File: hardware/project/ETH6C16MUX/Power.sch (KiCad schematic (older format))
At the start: 27 parts, among them Q701 IRFR5410, U701 OKI-T3-W40P-C, U702 MAX5902, U703 ADP7156ARDZ-3.3-R7, U704 LD1117S12TR_SOT223

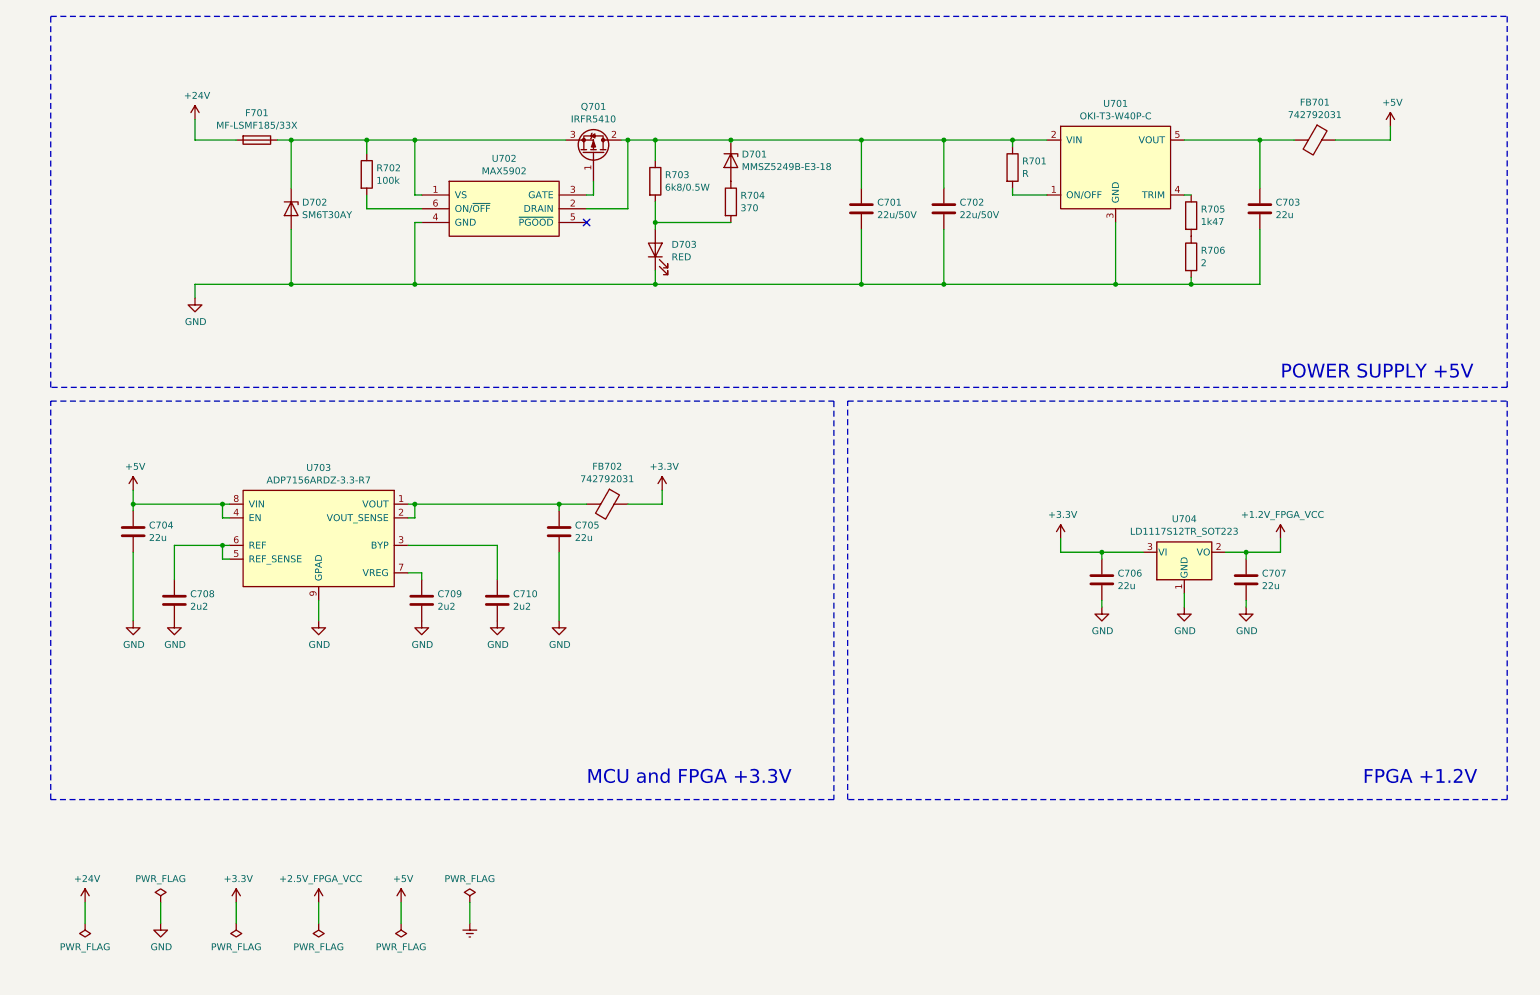
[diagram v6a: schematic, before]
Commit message: PCB layout, deleted USB.
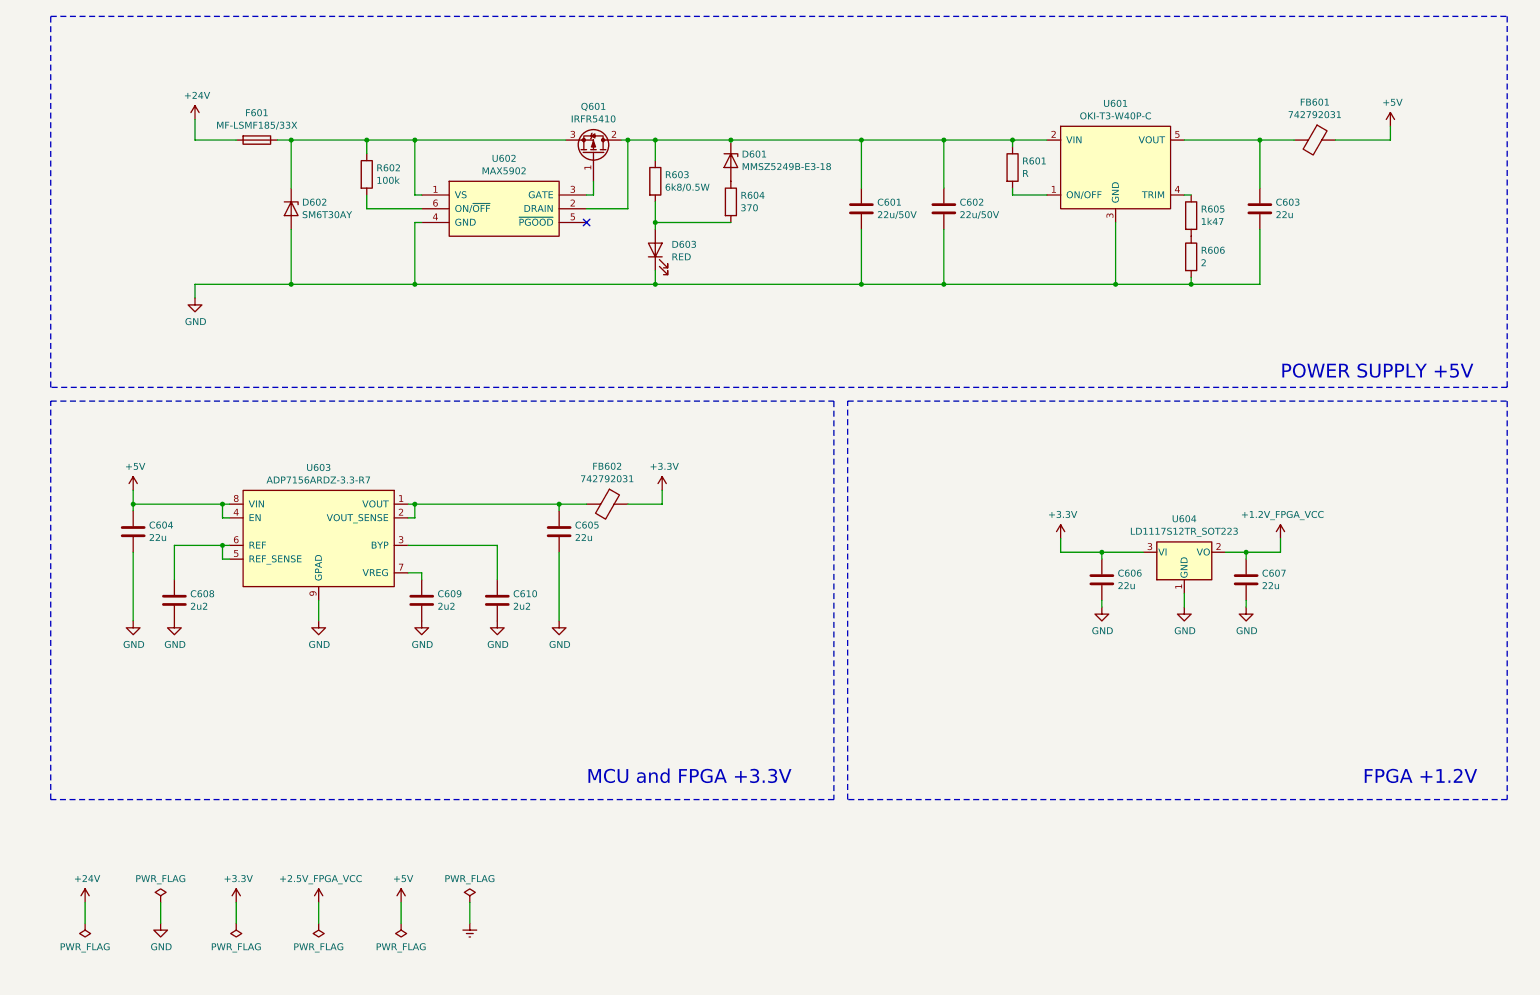
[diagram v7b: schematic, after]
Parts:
- renumbered C701 to C601, C702 to C602, C703 to C603, C704 to C604, C705 to C605, C706 to C606, C707 to C607, C708 to C608, C709 to C609, C710 to C610, D701 to D601, D702 to D602, D703 to D603, F701 to F601, FB701 to FB601, FB702 to FB602, Q701 to Q601, R701 to R601, R702 to R602, R703 to R603, R704 to R604, R705 to R605, R706 to R606, U701 to U601, U702 to U602, U703 to U603, U704 to U604

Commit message: Deleted FPGA part and change it for SPI IO chips. Change power supply circuit.
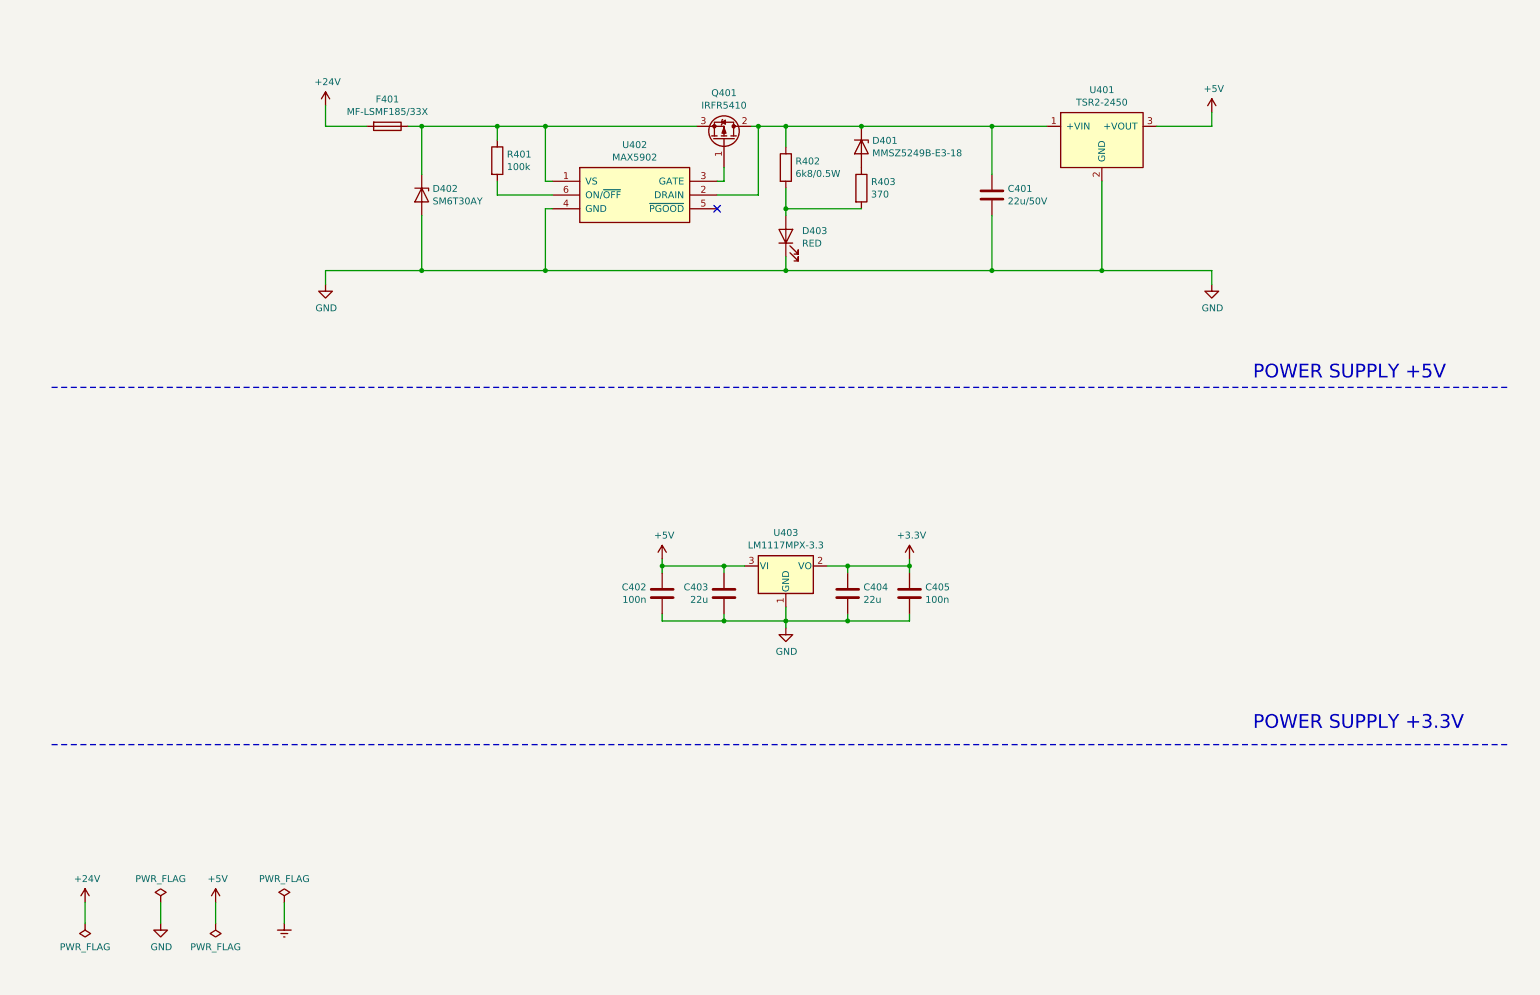
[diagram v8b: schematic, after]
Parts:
- removed C602: 22u/50V, Capacitor_SMD:C_2220_5650Metric_Pad1.97x5.40mm_HandSolder, symbol Device:C
- removed C603, C604, C605, C606, C607: 22u, ETH6C16MXU:C_1210_BB_3225Metric_Pad1.42x2.65mm_HandSolder, symbol Device:C
- removed C608, C609, C610: 2u2, ETH6C16MXU:C_0805_C_Pad1.15x1.40mm_HandSolder, symbol Device:C
- removed FB601, FB602: 742792031, ETH6C16MXU:R_0805_D_Pad1.15x1.40mm_HandSolder, symbol Device:Ferrite_Bead
- removed R601: R, Resistor_SMD:R_0603_1608Metric_Pad1.05x0.95mm_HandSolder, symbol Device:R
- removed R605: 1k47, Resistor_SMD:R_0603_1608Metric_Pad1.05x0.95mm_HandSolder, symbol Device:R
- removed R606: 2, Resistor_SMD:R_0603_1608Metric_Pad1.05x0.95mm_HandSolder, symbol Device:R
- removed U601: OKI-T3-W40P-C, ETH6C16MXU:OKI-T3-W40, symbol ETH6C16MUX:OKI-T3-W40P-C
- removed U603: ADP7156ARDZ-3.3-R7, Package_SO:SOIC-8-1EP_3.9x4.9mm_P1.27mm_EP2.41x3.81mm_ThermalVias, symbol ETH6C16MUX:ADP7156ARDZ-3.3-R7
- removed U604: LD1117S12TR_SOT223, Package_TO_SOT_SMD:SOT-223-3_TabPin2, symbol Regulator_Linear:LD1117S12TR_SOT223
- added C402, C405: 100n, Capacitor_SMD:C_0603_1608Metric_Pad1.05x0.95mm_HandSolder, symbol Device:C
- added C403, C404: 22u, Capacitor_SMD:C_1210_3225Metric_Pad1.42x2.65mm_HandSolder, symbol Device:C
- added U401: TSR2-2450, ETH6C16MXU:TSR2, symbol ETH6C16MUX:TSR2-2450
- added U403: LM1117MPX-3.3, Package_TO_SOT_SMD:SOT-223-3_TabPin2, symbol Regulator_Linear:LM1117-3.3
- renumbered C601 to C401, D601 to D401, D602 to D402, D603 to D403, F601 to F401, Q601 to Q401, R602 to R401, R603 to R402, R604 to R403, U602 to U402
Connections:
- net +3V3: now also C404.1, C405.1, U403.2 (VO)
- net +5V: now also C402.1, C403.1, U401.3 (+VOUT), U403.3 (VI)
- net GND: now also C402.2, C403.2, C404.2, C405.2, U401.2 (GND), U403.1 (GND)
- net at C401.1, D401.1 (K), Q401.2 (D)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: now also U401.1 (+VIN)
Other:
- note added: "POWER SUPPLY +3.3V"
- note removed: "FPGA +1.2V\n"
- note removed: "MCU and FPGA +3.3V"
- moved on the sheet: C401, D401, D402, D403, F401, Q401, R401, R402, R403, U402
